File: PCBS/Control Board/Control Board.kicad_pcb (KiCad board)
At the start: 2 copper layers, 29.6 x 48.1 mm, 24 parts, among them J1 S3B-PH-K-S(LF)(SN), J2 Conn_02x03_Odd_Even, J3 S2B-PH-K-S(LF)(SN), U1 ATmega328-MM, U2 RP400N501A-TR-FE, U3 LDL1117, U4 TXU0304, U5 HP203B, Y1 Resonator

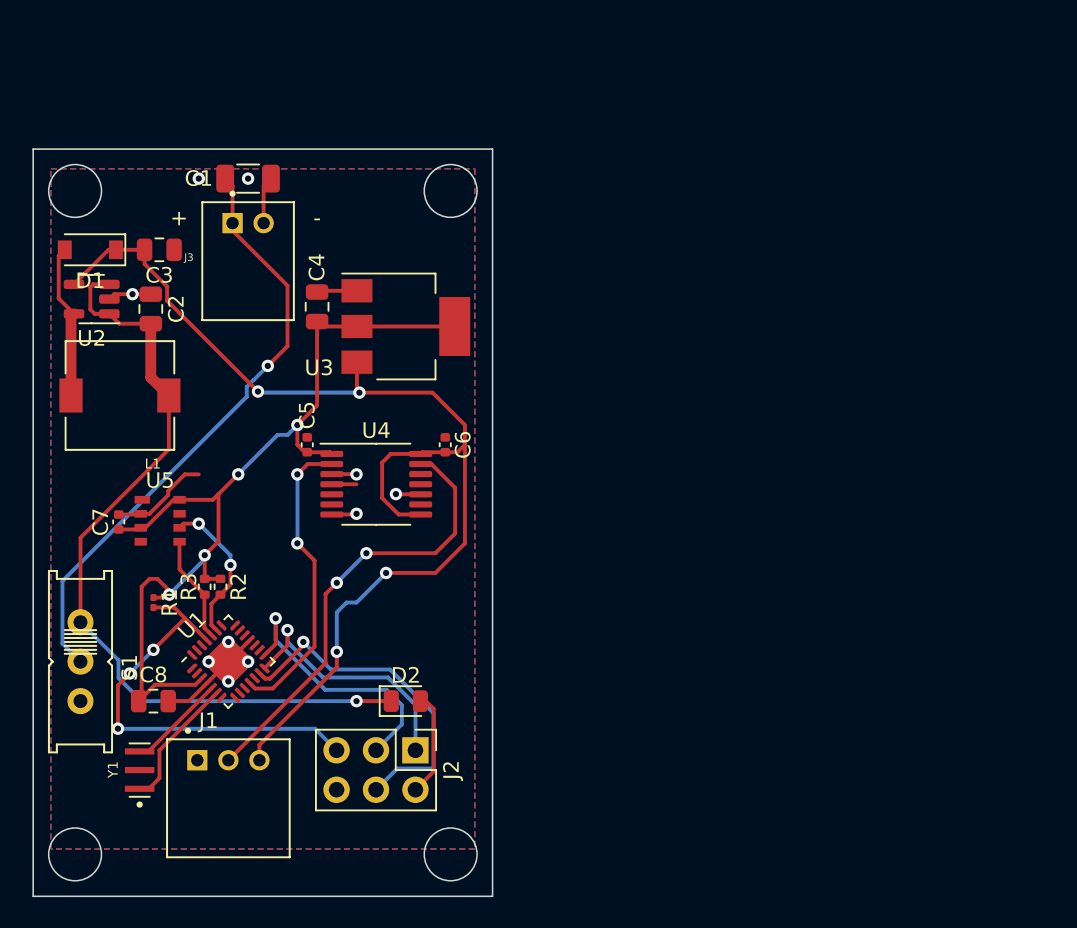
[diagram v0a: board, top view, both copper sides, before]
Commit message: Updated schematic, started updating layout
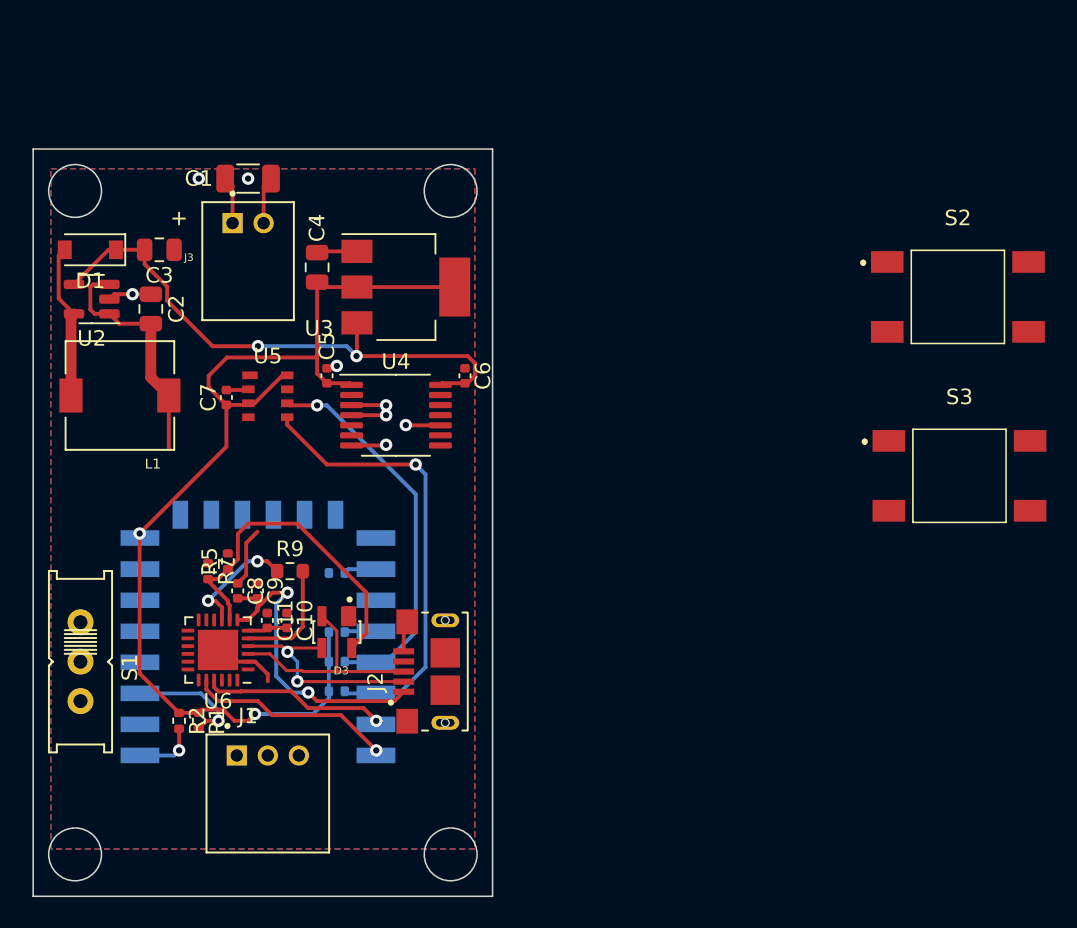
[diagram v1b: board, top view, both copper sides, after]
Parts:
- removed D2: D, Diode_SMD:D_0805_2012Metric
- removed Y1: Resonator, CSTNE16M0V530000R0:OSC_CSTNE16M0V530000R0
- added C10: 4.7uF, Capacitor_SMD:C_0402_1005Metric, F.Cu at (135.9, 110.4)
- added C11: 0.1uF, Capacitor_SMD:C_0402_1005Metric, F.Cu at (134.6, 110.4)
- added C9: 0.1uF, Capacitor_SMD:C_0402_1005Metric, F.Cu at (134.0, 108.5)
- added D3: SP0503BAHTG, SP0503BAHTG:SOT143, F.Cu at (139.1, 111.1)
- added R4: 4.7k, Resistor_SMD:R_0402_1005Metric, B.Cu at (139.1, 114.9)
- added R5: 47.5k, Resistor_SMD:R_0402_1005Metric, F.Cu at (132.0, 106.6)
- added R6: 4.7k, Resistor_SMD:R_0402_1005Metric, B.Cu at (139.1, 113.0)
- added R7: 22.1k, Resistor_SMD:R_0402_1005Metric, F.Cu at (130.8, 107.2)
- added R8: 10k, Resistor_SMD:R_0402_1005Metric, B.Cu at (139.1, 111.1)
- added R9: 1k, Resistor_SMD:R_0603_1608Metric, F.Cu at (136.0, 107.2)
- added S2: TL3301AF260QG, TL3301AF260QG Pushbutton:TL3301AF260QG, F.Cu at (179.1, 89.5)
- added S3: TL3301AF260QG, TL3301AF260QG Pushbutton:TL3301AF260QG, F.Cu at (179.2, 101.1)
- added U6: CP2102N-Axx-xQFN24, Package_DFN_QFN:QFN-24-1EP_4x4mm_P0.5mm_EP2.6x2.6mm, F.Cu at (131.4, 112.3)
- C8: value 10uF -> 4.7uF; footprint Capacitor_SMD:C_0805_2012Metric -> Capacitor_SMD:C_0402_1005Metric
- J2: value Conn_02x03_Odd_Even -> 10118193-0001LF; footprint Connector_PinHeader_2.54mm:PinHeader_2x03_P2.54mm_Vertical -> 10118193-0001LF Micro B Port:FCI_10118193-0001LF
- R1: footprint Resistor_SMD:R_0201_0603Metric -> Resistor_SMD:R_0402_1005Metric
- R2: value 4.7K -> 10k
- R3: value 4.7k -> 10k; moved to B.Cu
- U1: value ATmega328-MM -> ESP-12F; footprint Package_DFN_QFN:QFN-28-1EP_4x4mm_P0.45mm_EP2.4x2.4mm -> RF_Module:ESP-12E; moved to B.Cu
- moved C7 10.6 mm to (132.0, 96.0)
- moved U5 10.6 mm to (134.6, 95.9)
- moved R2 9.04 mm to (128.9, 116.8)
- moved C8 8.94 mm to (132.7, 108.5), turned to -90 degrees
- moved R3 8.56 mm to (139.1, 107.3), turned to 180 degrees
- moved R1 8.16 mm to (130.2, 116.8)
- moved J2 5.43 mm to (146.1, 113.7), turned to 90 degrees
- moved C5 4.62 mm to (138.4, 94.6)
- moved C6 4.62 mm to (147.3, 94.6)
- moved U4 4.62 mm to (142.9, 97.2)
- moved U1 3.17 mm to (134.0, 115.6), turned to 0 degrees
- moved J1 2.56 mm to (132.6, 119.1)
- moved C4 2.54 mm to (137.8, 87.6)
- moved U3 2.54 mm to (143.5, 88.9)
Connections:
- C8 pad 1: +3V3 -> GND
- C8 pad 2: GND -> Net-(C8-Pad2)
- J2 pad 1: /MISO -> Net-(C8-Pad2)
- J2 pad 2: /ICSP_VCC -> /D-
- J2 pad 3: /SCK -> /D+
- J2 pad 4: /MOSI -> unconnected-(J2-Pad4)
- J2 pad 5: /RST -> GND
- R1 pad 2: /RST -> Net-(R1-Pad2)
- R2 pad 2: /SDA -> Net-(R2-Pad2)
- R3 pad 1: +3V3 -> Net-(R3-Pad1)
- R3 pad 2: /SCL -> GND
- U1 pad 1: unconnected-(U1-Pad1) -> Net-(R2-Pad2)
- U1 pad 11: Net-(U1-Pad11) -> unconnected-(U1-Pad11)
- U1 pad 13: /MOSI -> unconnected-(U1-Pad13)
- U1 pad 14: /MISO -> unconnected-(U1-Pad14)
- U1 pad 15: /SCK -> GND
- U1 pad 16: unconnected-(U1-Pad16) -> Net-(R3-Pad1)
- U1 pad 17: unconnected-(U1-Pad17) -> /GPIO2
- U1 pad 18: GND -> Net-(R8-Pad2)
- U1 pad 19: unconnected-(U1-Pad19) -> /SDA
- U1 pad 20: unconnected-(U1-Pad20) -> /SCL
- U1 pad 21: unconnected-(U1-Pad21) -> /ESP_RX
- U1 pad 22: unconnected-(U1-Pad22) -> /ESP_TX
- U1 pad 3: +3V3 -> Net-(R1-Pad2)
- U1 pad 4: GND -> unconnected-(U1-Pad4)
- U1 pad 5: Net-(U1-Pad5) -> unconnected-(U1-Pad5)
- U1 pad 6: Net-(U1-Pad6) -> unconnected-(U1-Pad6)
- U1 pad 8: unconnected-(U1-Pad8) -> +3V3
- U4 pad 2: Net-(U1-Pad11) -> /GPIO2
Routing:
- net Net-(C2-Pad1): track 52.5 -> 16.2 mm, vias 1 -> 0
- net Net-(C1-Pad1): track 39.1 -> 3.06 mm, vias 1 -> 0
- net +5V: track 74.2 -> 38.6 mm, vias 4 -> 2
- net /DO: track 29.1 -> 0.00 mm, vias 2 -> 0
- net /RST: track 27.9 -> 0.00 mm, vias 3 -> 0
- net /MOSI: track 22.2 -> 0.00 mm, vias 1 -> 0
- net /SCL: track 6.91 -> 29.1 mm, vias 0 -> 1
- net Net-(D3-Pad4): track 0.00 -> 21.6 mm
- net Net-(C8-Pad2): track 0.00 -> 21.1 mm, vias 0 -> 2
- net Net-(U1-Pad11): track 19.5 -> 0.00 mm, vias 2 -> 0
- net /SCK: track 17.5 -> 0.00 mm, vias 1 -> 0
- net /MISO: track 16.7 -> 0.00 mm, vias 1 -> 0
- net /SDA: track 9.73 -> 25.0 mm, vias 2 -> 1
- net /D+: track 0.00 -> 14.5 mm
- net /D-: track 0.00 -> 14.0 mm, vias 0 -> 2
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
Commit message: Completed switch to ESP-12F
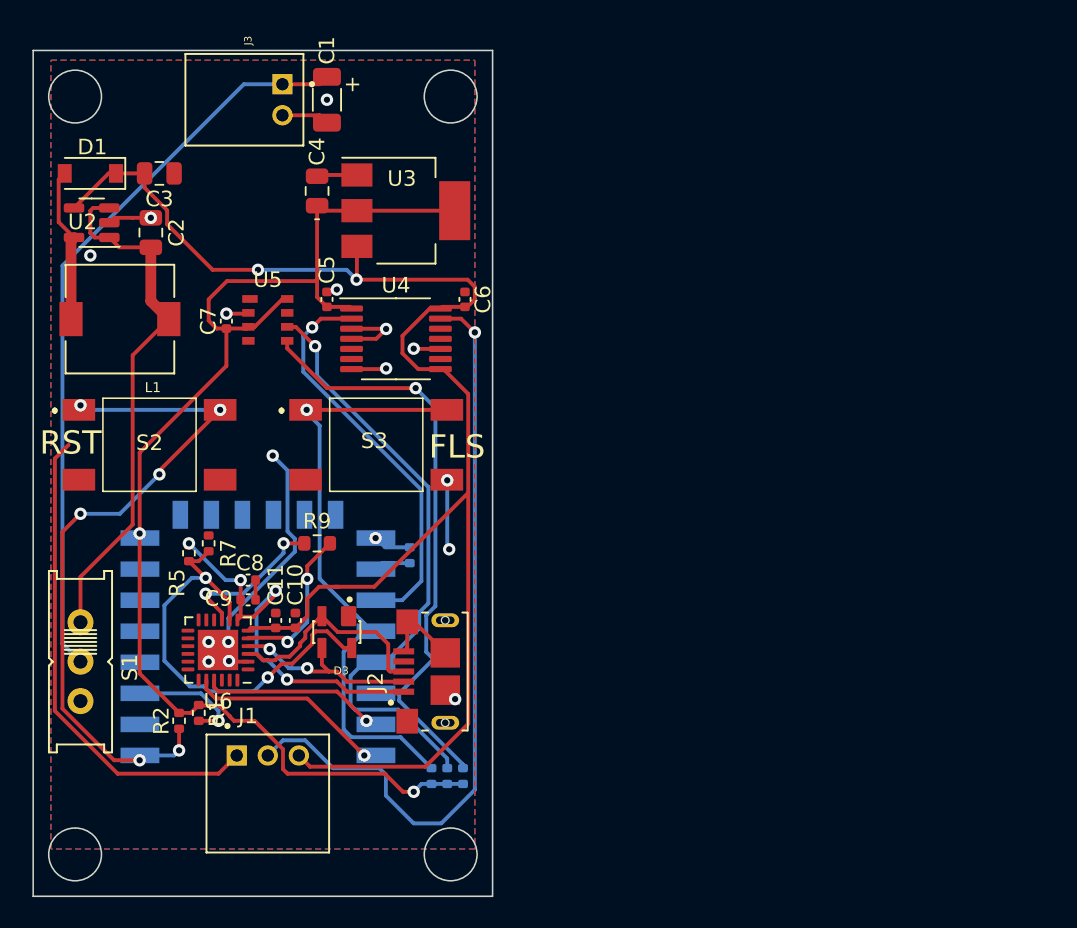
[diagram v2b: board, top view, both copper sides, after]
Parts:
- moved S2 52.9 mm to (127.0, 99.1)
- moved S3 37.6 mm to (141.6, 99.1)
- moved R8 11.1 mm to (145.2, 120.4), turned to 90 degrees
- moved R6 10.2 mm to (146.2, 120.4), turned to 90 degrees
- moved R4 9.79 mm to (147.2, 120.4), turned to 90 degrees
- moved J3 8.25 mm to (135.6, 76.8), turned to -90 degrees
- moved C1 7.18 mm to (138.4, 76.8), turned to -90 degrees
- moved C2 4.92 mm to (127.1, 85.4)
- moved C3 4.92 mm to (127.6, 81.6)
- moved C4 4.92 mm to (137.8, 82.7)
- moved C5 4.92 mm to (138.4, 89.7)
- moved C6 4.92 mm to (147.3, 89.7)
- moved C7 4.92 mm to (132.0, 91.1)
- moved D1 4.92 mm to (123.2, 81.6)
- moved L1 4.92 mm to (125.1, 91.0)
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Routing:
- net +5V: track 38.6 -> 98.5 mm
- net GND: track 29.0 -> 81.2 mm, vias 8 -> 17
- net /DO: track 0.00 -> 49.7 mm, vias 0 -> 1
- net Net-(C1-Pad1): track 3.06 -> 48.1 mm
- net Net-(R2-Pad2): track 4.05 -> 44.5 mm, vias 1 -> 6
- net Net-(R8-Pad2): track 2.03 -> 39.6 mm, vias 0 -> 1
- net /GPIO2: track 0.00 -> 25.9 mm, vias 0 -> 1
- net Net-(C2-Pad1): track 16.2 -> 34.0 mm
- net /SDA: track 25.0 -> 39.6 mm
- net +3V3: track 70.1 -> 82.3 mm
- net /SCL: track 29.1 -> 39.4 mm
- net Net-(D3-Pad4): track 21.6 -> 28.6 mm, vias 0 -> 2
- net Net-(C8-Pad2): track 21.1 -> 25.1 mm, vias 2 -> 4
- net /2102N VIO: track 7.43 -> 10.1 mm, vias 0 -> 2
- net Net-(R9-Pad1): track 7.63 -> 10.2 mm
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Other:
- board size 29.6 x 48.1 mm -> 29.6 x 54.5 mm
- board text added: "FLS"
- board text added: "RST"
